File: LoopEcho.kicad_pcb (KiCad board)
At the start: 2 copper layers, 100 x 83.5 mm, 87 parts, among them J1 IJ/IN/LED/GND/OUT/OJ, J2 INPUT, J3 OUTPUT, J4 SEND, J5 RETURN, J6 DC 9V, U1 PT2399, U2 TL072, U3 TL072, U4 LM358, U5 AMS1117-5.0

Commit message: Two footswitches: LOOP (left) switches the effects loop, BYPASS (right)
- Schematic: J7 header for a second SwitchPCB v2 wired as a loop selector
  (IJ = SEND, IN = SEND jack, LED = LOOP LED D7 / R33, OUT = RETURN jack, OJ = RET).
  Loop off: RET = SEND and the SEND jack is grounded. ERC 0.
- Board (hand-edited, reworked in place): second notch, both headers beside their
  notches like the user's J1, LEDs at X +-28 / Y -14.2, U1 / U2 / U4 groups
  re-placed, re-routed: DRC 0 errors / 0 unconnected, parity clean, 47 vias.
- buildpcb_loopecho.py marked out of date.

Co-Authored-By: Claude Opus 5.5 <noreply@anthropic.com>
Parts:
- added D7: LED, LED_THT:LED_D3.0mm, B.Cu at (176.7, 114.2)
- added J7: LOOP SW, Connector_PinHeader_2.54mm:PinHeader_1x06_P2.54mm_Vertical, F.Cu at (165.8, 132.0)
- added R33: 4k7, Resistor_SMD:R_0805_2012Metric_Pad1.20x1.40mm_HandSolder, F.Cu at (176.5, 110.5)
- moved R8 42.6 mm to (145.5, 133.0), turned to 0 degrees
- moved R14 37.9 mm to (140.8, 131.5)
- moved C21 32.6 mm to (142.8, 118.8)
- moved R10 32.0 mm to (144.5, 129.2), turned to 90 degrees
- moved C13 31.3 mm to (137.0, 129.2)
- moved R4 30.7 mm to (137.8, 116.8), turned to 0 degrees
- moved R6 30.4 mm to (142.2, 114.8)
- moved R5 30.1 mm to (134.2, 129.5), turned to 90 degrees
- moved J1 28.0 mm to (109.8, 132.0)
- moved D6 28.0 mm to (120.7, 114.2)
- moved C10 27.7 mm to (141.0, 128.5)
- moved C11 27.7 mm to (139.0, 119.5)
- moved U2 27.7 mm to (140.0, 124.0)
- moved C20 27.0 mm to (148.8, 125.2), turned to 0 degrees
- moved R9 26.8 mm to (133.8, 115.5)
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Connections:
- J4 pad T: /SEND -> /SENDJ
- J5 pad T: /RET -> /RETJ
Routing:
- net GND: track 394.1 -> 490.3 mm, vias 10 -> 3
- net /SENDJ: track 0.00 -> 84.6 mm
- net /DIN: track 117.3 -> 41.5 mm
- net /RETJ: track 0.00 -> 50.4 mm
- net /SEND: track 92.6 -> 138.8 mm
- net /OJ: track 71.6 -> 110.3 mm
- net Net-(D6-A): track 28.2 -> 57.7 mm, vias 1 -> 0
- net /VCO: track 36.2 -> 58.8 mm, vias 1 -> 2
- net Net-(C31-Pad2): track 31.6 -> 9.81 mm
- net Net-(U4A--): track 30.7 -> 8.88 mm
- net /LED2_K: track 0.00 -> 21.7 mm
- net Net-(D1-A): track 52.1 -> 32.6 mm
- net +9V: track 134.7 -> 152.9 mm
- net /VB: track 142.9 -> 125.6 mm, vias 2 -> 6
- net /IN: track 36.9 -> 54.2 mm, vias 0 -> 2
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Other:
- outline, holes or cut-outs redrawn
- board text added: "BYPASS"
- board text added: "LOOP"

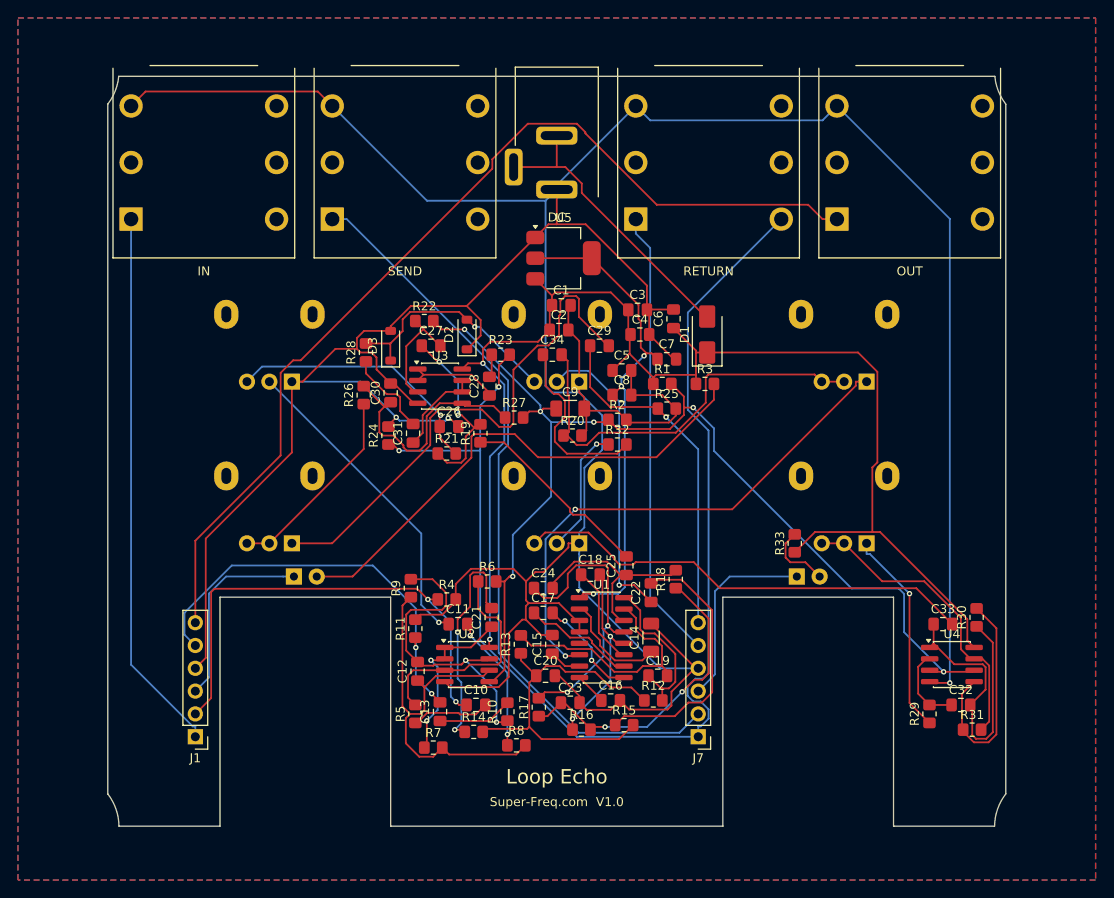
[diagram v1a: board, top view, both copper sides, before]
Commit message: Re-route with the 0.4 mm Power net class restored
Power class back in LoopEcho.kicad_pro (+9V, GND, +5V, /VB, D1-A; Default 0.25 mm; ERC and sch rev restored),
board re-routed (placement kept, 88 vias, DRC 0/0, parity clean); buildpcb now restores the .kicad_pro at exit.

Co-Authored-By: Claude Opus 5.5 <noreply@anthropic.com>
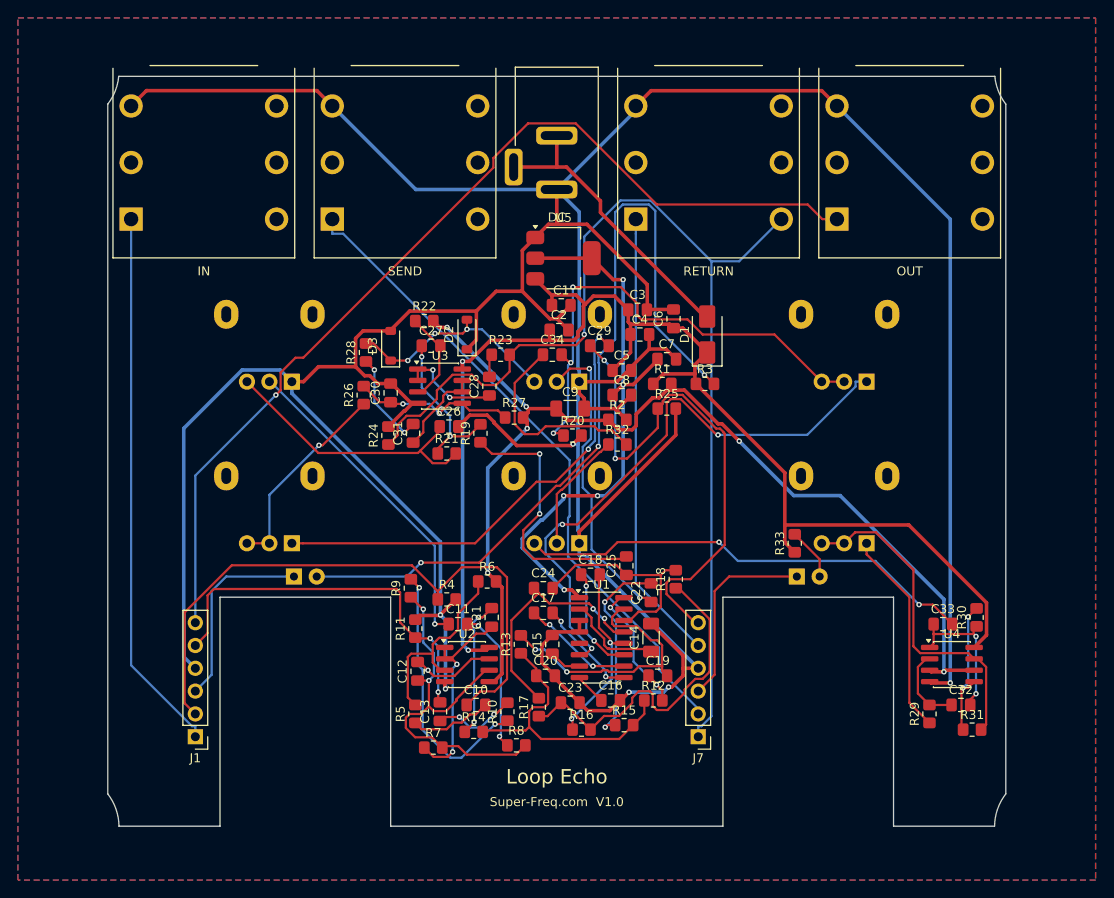
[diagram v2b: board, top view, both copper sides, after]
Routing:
- net Net-(D6-A): track 57.7 -> 91.5 mm, vias 0 -> 3
- net /RET: track 38.8 -> 58.8 mm, vias 1 -> 2
- net /TRI: track 33.3 -> 16.5 mm, vias 0 -> 2
- net /IN: track 54.2 -> 70.6 mm, vias 2 -> 0
- net /SEND: track 138.8 -> 123.4 mm, vias 2 -> 1
- net /SENDJ: track 84.6 -> 72.8 mm
- net Net-(C21-Pad2): track 25.4 -> 15.4 mm
- net Net-(U4B-+): track 25.7 -> 15.8 mm, vias 0 -> 2
- net GND: track 490.3 -> 499.9 mm, vias 3 -> 6
- net /DIN: track 41.5 -> 32.5 mm
- net Net-(C25-Pad2): track 21.7 -> 30.5 mm, vias 0 -> 2
- net /TMIN: track 46.4 -> 55.1 mm, vias 0 -> 3
- net Net-(U3B-+): track 26.9 -> 18.1 mm, vias 0 -> 2
- net +5V: track 55.2 -> 63.5 mm, vias 3 -> 5
- net Net-(C22-Pad2): track 29.8 -> 22.2 mm, vias 0 -> 2
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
